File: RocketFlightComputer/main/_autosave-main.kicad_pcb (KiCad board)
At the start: 4 copper layers, 53.7 x 53.7 mm, 128 parts, among them J1 BATT, Q2 SI2302, Q3 SI2302, Q4 SI2302, Y1 32.768kHz, Y2 24MHz, Y3 32.768kHz, Y4 32.768kHz

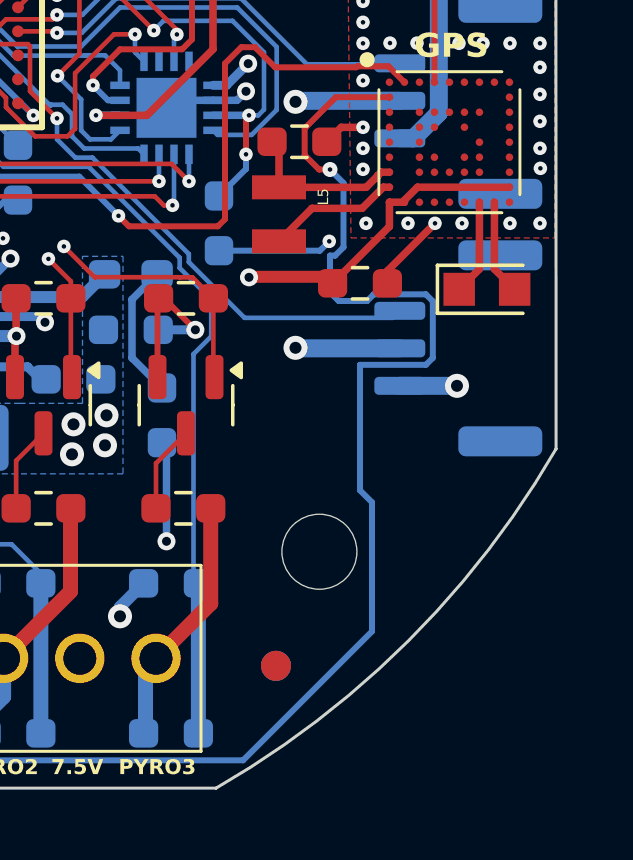
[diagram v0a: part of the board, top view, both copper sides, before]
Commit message: Layout changes to incorporate power capacitors for the servos
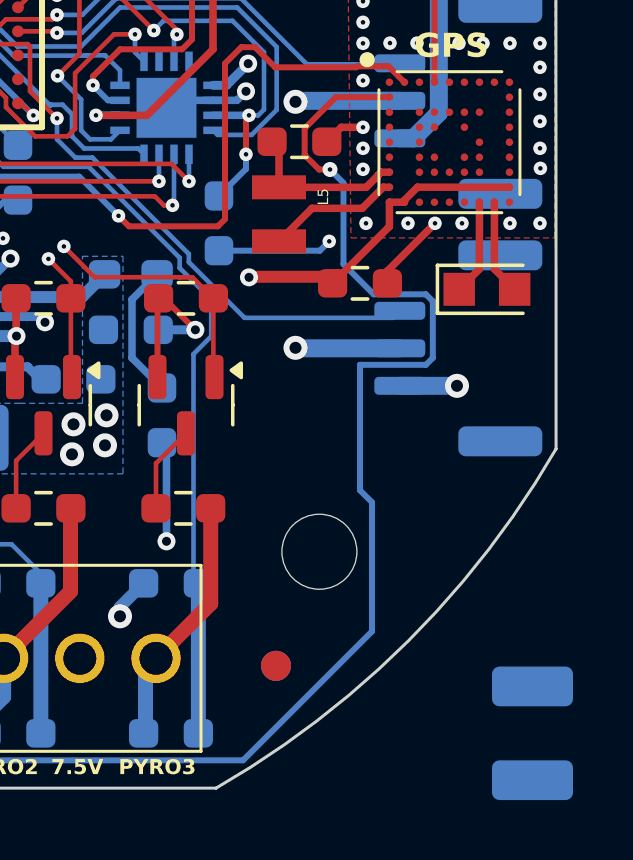
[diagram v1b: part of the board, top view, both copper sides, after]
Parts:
- added C41: 1000uf, Capacitor_SMD:C_1210_3225Metric_Pad1.33x2.70mm_HandSolder, B.Cu at (135.9, 83.5)
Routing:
- net /BMP390_SCL1: track 115.7 -> 114.2 mm
